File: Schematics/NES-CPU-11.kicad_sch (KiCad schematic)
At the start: 121 parts, among them P1 72-Pin Connector, P2 EXP-Connector, P3 MOD RF, P4 Controller Input, P5 Controller Input, P6 PWR/RST IN, Q1 2SA937, Q2 2SC2021, Q3 2SC2021, U1 6116 (WRAM), U10 CIC, U2 74HC373, U3 74HC139, U4 6116 (VRAM), U5 RP2C02 PPU, U6 RP2A03 CPU, U7 40H368 (CI), U8 40H368 (CII), U9 74LS04, X1 21.477272 MHz, X2 4MHz

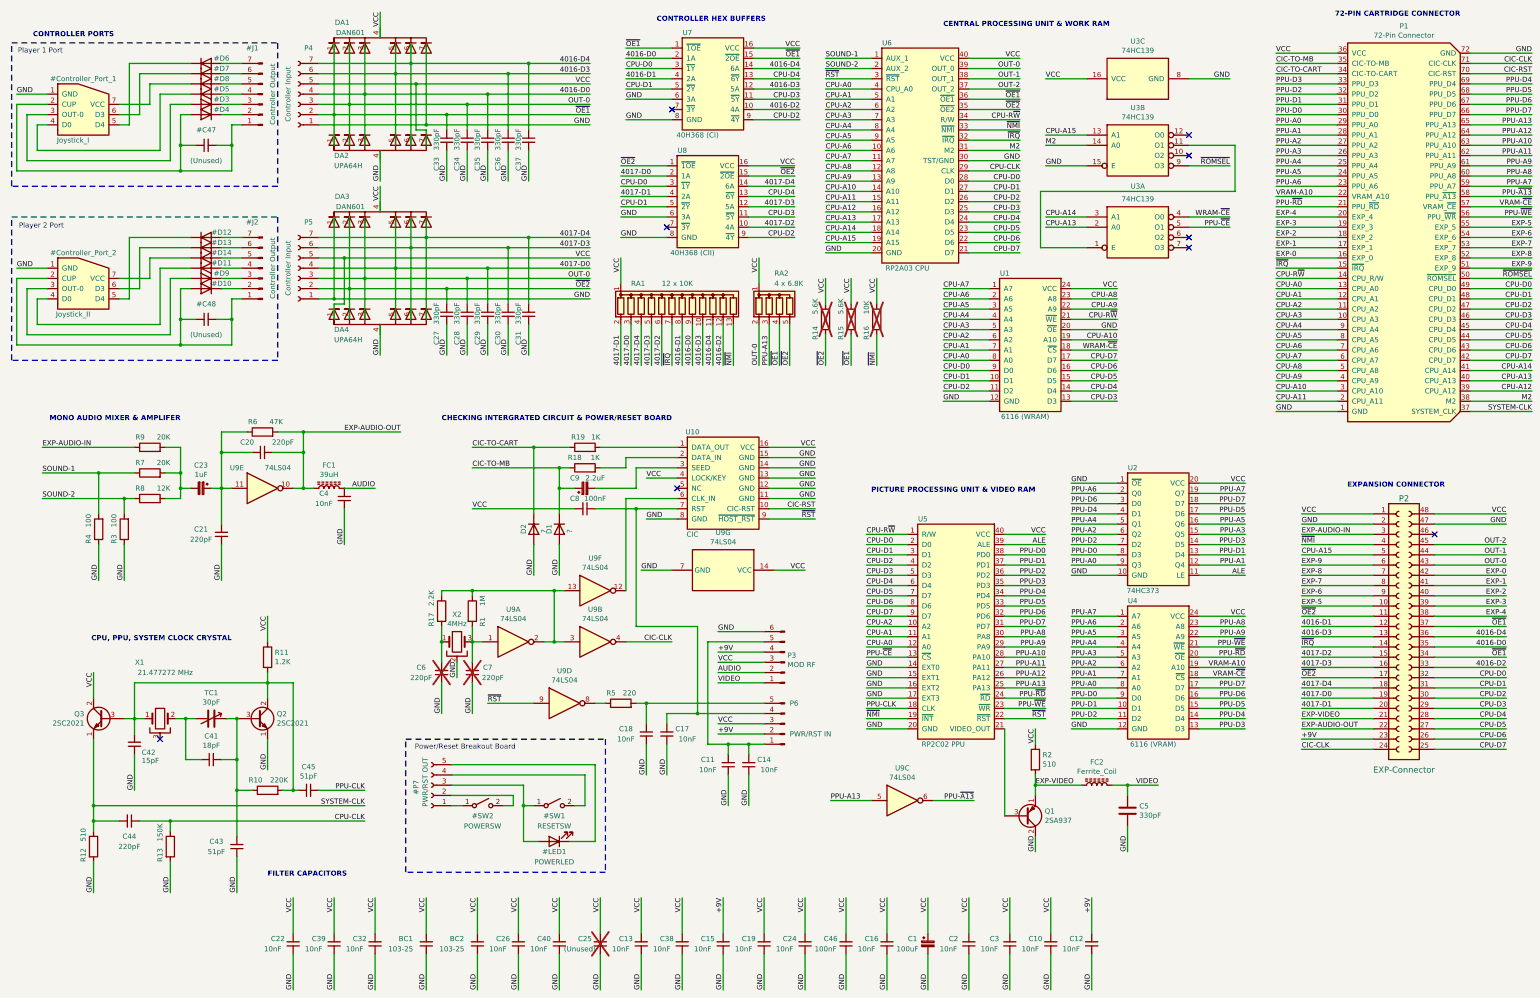
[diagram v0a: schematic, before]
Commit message: + Migrate files in Schematics/ folder to Kicad 9 + Correct all instances of "CONTROLLER SHIFT REGISTERS" in main schematic and files in Schematics/ folder to "CONTROLLER HEX BUFFERS" + Fix symbol issues caused by Kicad 6+ library and symbol name changes + Fix a few instances of net labels being connected to pins without a leading wire in all schematics (This is aesthetic, it looked bad)
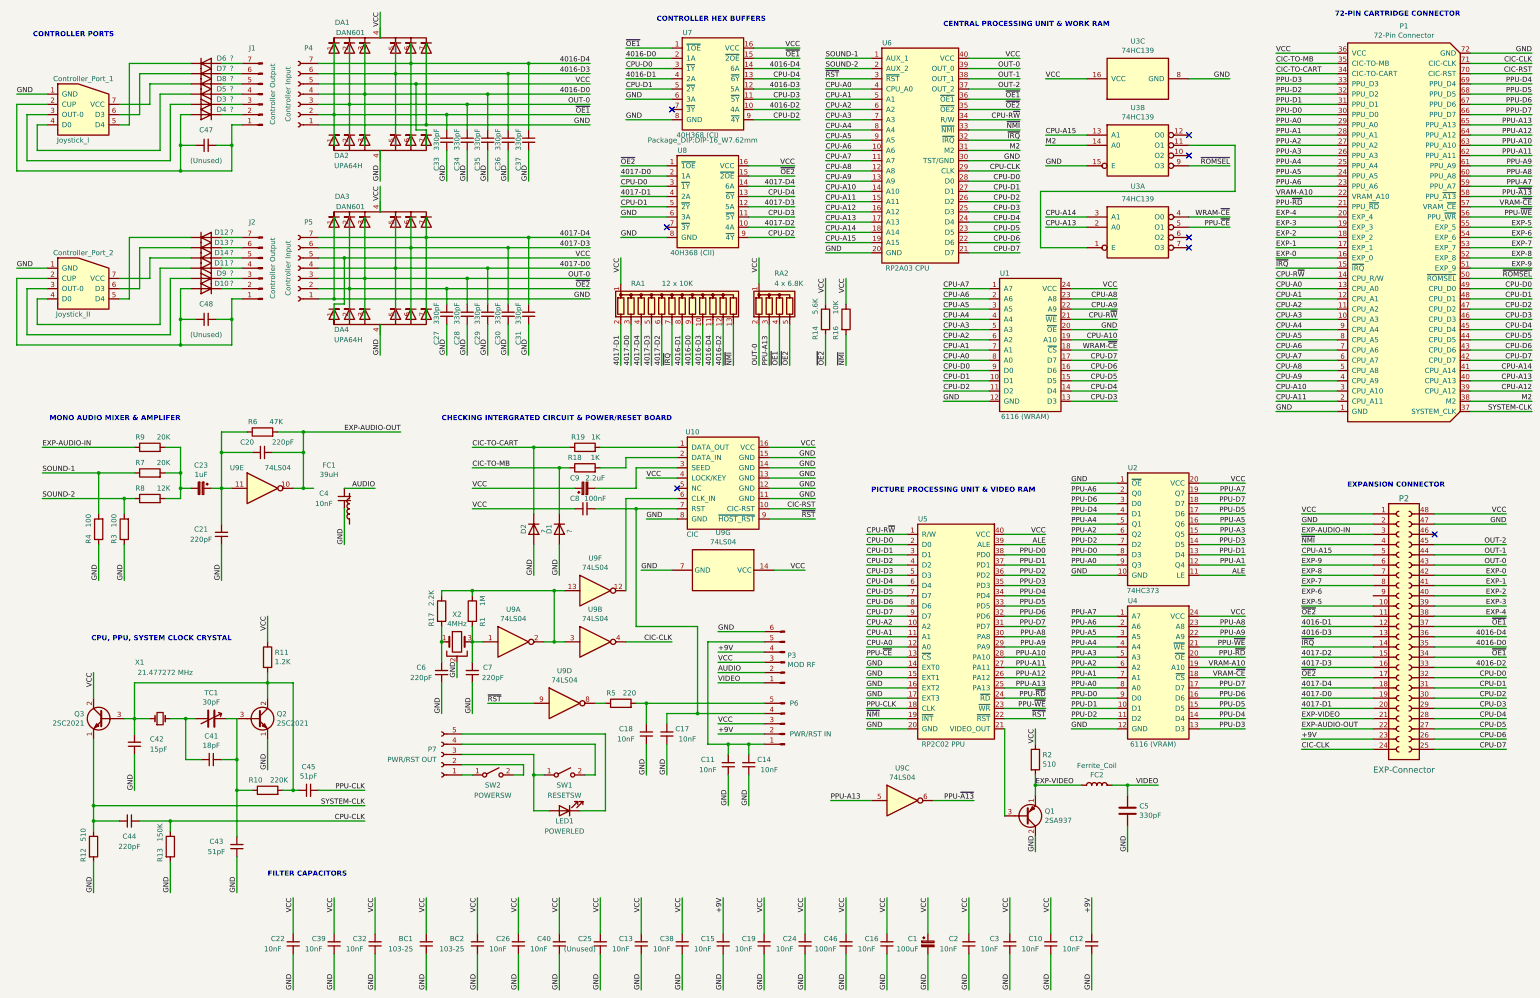
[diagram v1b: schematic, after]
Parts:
- removed R15: 5.6K, Resistor_THT:R_Axial_DIN0207_L6.3mm_D2.5mm_P10.16mm_Horizontal, symbol Device:R
- C25, C6, C7, R14, R16: now fitted; now in the parts list
- C4: footprint Capacitor_THT:C_Disc_D5.0mm_W2.5mm_P5.00mm -> Capacitor_THT:C_Disc_D3.0mm_W1.6mm_P2.50mm
- FC1, FC2: symbol Device:L_Ferrite -> Motherboard:Ferrite_Core
- Q1: footprint NESRE:TO-126-3_Vertical_Short -> Package_TO_SOT_THT:TO-126-3_Vertical; symbol Device:Q_PNP_ECB -> Transistor_BJT:Q_PNP_ECB
- Q2, Q3: footprint NESRE:TO-126-3_Vertical_Short -> Package_TO_SOT_THT:TO-126-3_Vertical; symbol Device:Q_NPN_ECB -> Transistor_BJT:Q_NPN_ECB
- U1, U4: footprint NESRE:DIP-24_W15.24-7.62mm -> Package_DIP:DIP-24_W7.62mm
- X1: symbol Device:Crystal_GND3 -> Device:Crystal_Small
- X2: footprint Crystal:Resonator_Murata_CSTLSxxxG-3Pin_W8.0mm_H3.0mm -> Crystal:Resonator_muRata_CSTLSxxxG-3Pin_W8.0mm_H3.0mm
- renumbered #C47 to C47, #C48 to C48, #Controller_Port_1 to Controller_Port_1, #Controller_Port_2 to Controller_Port_2, #D10 to D10, #D11 to D11, #D12 to D12, #D13 to D13, #D14 to D14, #D3 to D3, #D4 to D4, #D5 to D5, #D6 to D6, #D7 to D7, #D8 to D8, #D9 to D9, #J1 to J1, #J2 to J2, #LED1 to LED1, #P7 to P7, #SW1 to SW1, #SW2 to SW2
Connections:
- net AUDIO: no longer FC1.2
- net CIC-TO-MB: no longer C9.1
- net EXP-6: no longer P2.9
- net EXP-AUDIO-OUT: no longer FC1.1
- net EXP-VIDEO: now also FC2.~; no longer FC2.1
- net VCC: now also C9.1
- net VIDEO: now also FC2.~; no longer FC2.2
- no-connect marks 9 -> 8
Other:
- note removed: "Player 1 Port"
- note removed: "Player 2 Port"
- note removed: "Power/Reset Breakout Board"
